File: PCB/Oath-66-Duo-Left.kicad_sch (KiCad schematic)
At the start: 67 parts, among them U1 Arduino_Pro_Micro

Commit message: PCB Updated
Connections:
- net Col 0: now also U1.16 (15/PB1); no longer U1.8 (5/PC6)
- net Col 1: now also U1.5 (2/PD1); no longer U1.10 (7/PE6)
- net Col 2: now also U1.7 (4/PD4); no longer U1.11 (8/PB4)
- net Col 3: now also U1.9 (6/PD7); no longer U1.15 (14/PB3)
- net Col 4: now also U1.11 (8/PB4); no longer U1.13 (10/PB6)
- net Col 5: now also U1.13 (10/PB6); no longer U1.5 (2/PD1)
- net Col 6: now also U1.14 (16/PB2); no longer U1.6 (3/PD0)
- net Row 0: now also U1.15 (14/PB3); no longer U1.7 (4/PD4)
- net Row 1: now also U1.6 (3/PD0); no longer U1.9 (6/PD7)
- net Row 2: now also U1.8 (5/PC6); no longer U1.12 (9/PB5)
- net Row 3: now also U1.10 (7/PE6); no longer U1.16 (15/PB1)
- net Row 4: now also U1.12 (9/PB5); no longer U1.14 (16/PB2)

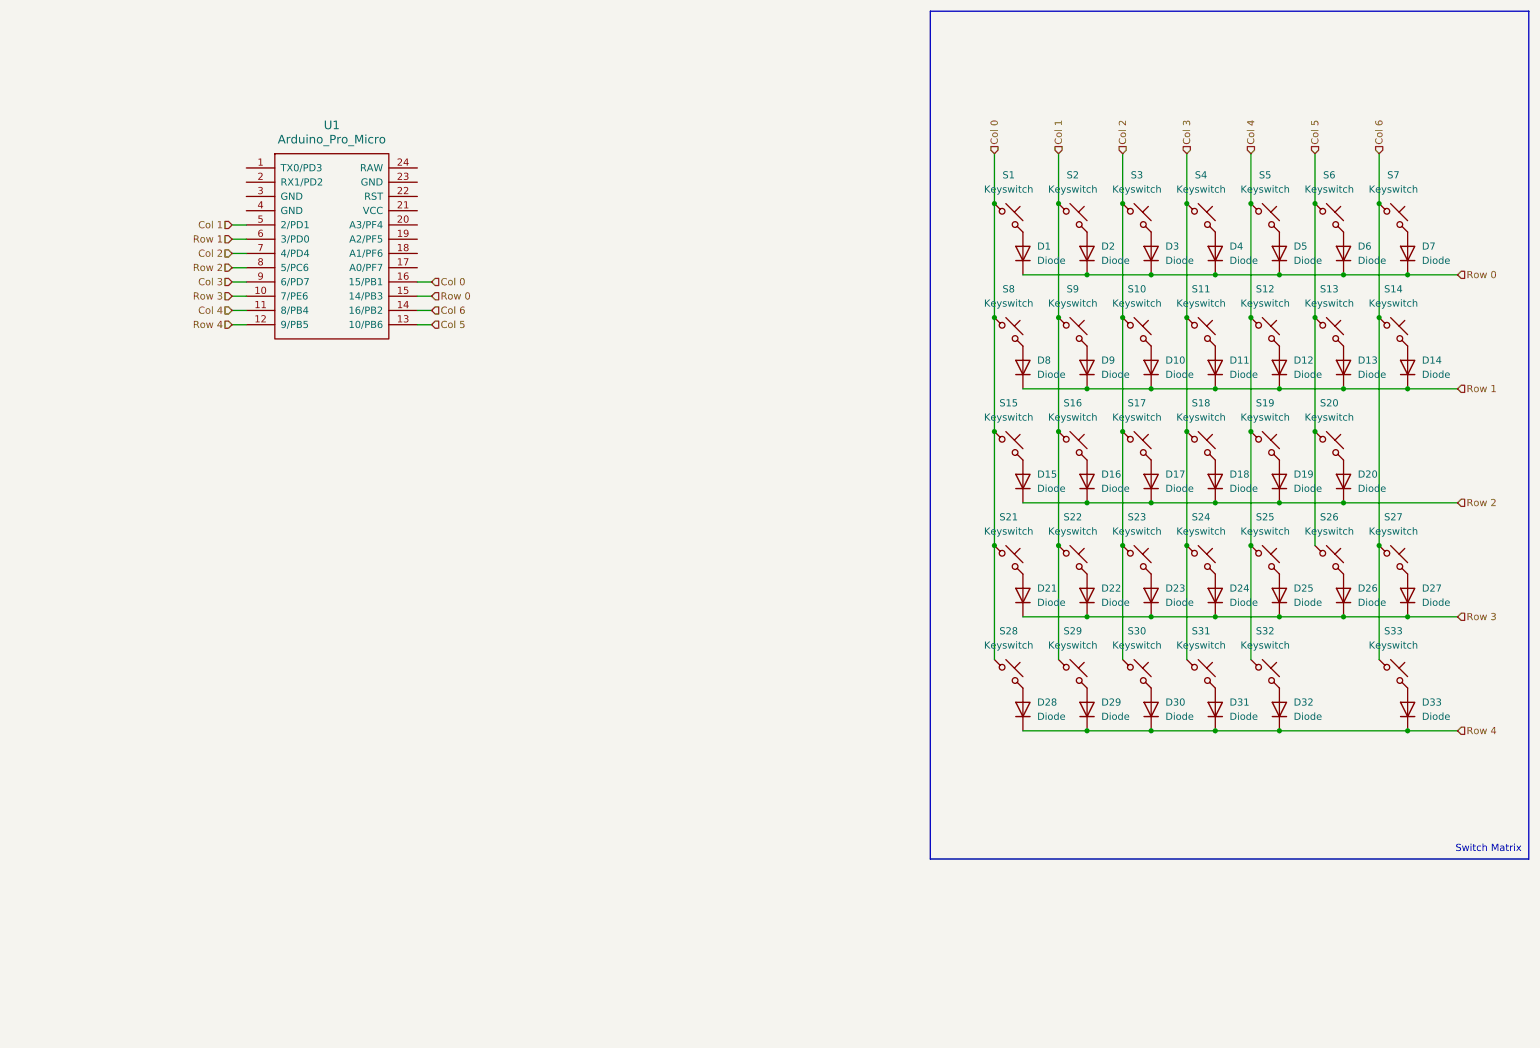
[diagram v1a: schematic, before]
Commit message: Schematic and PCB Updated
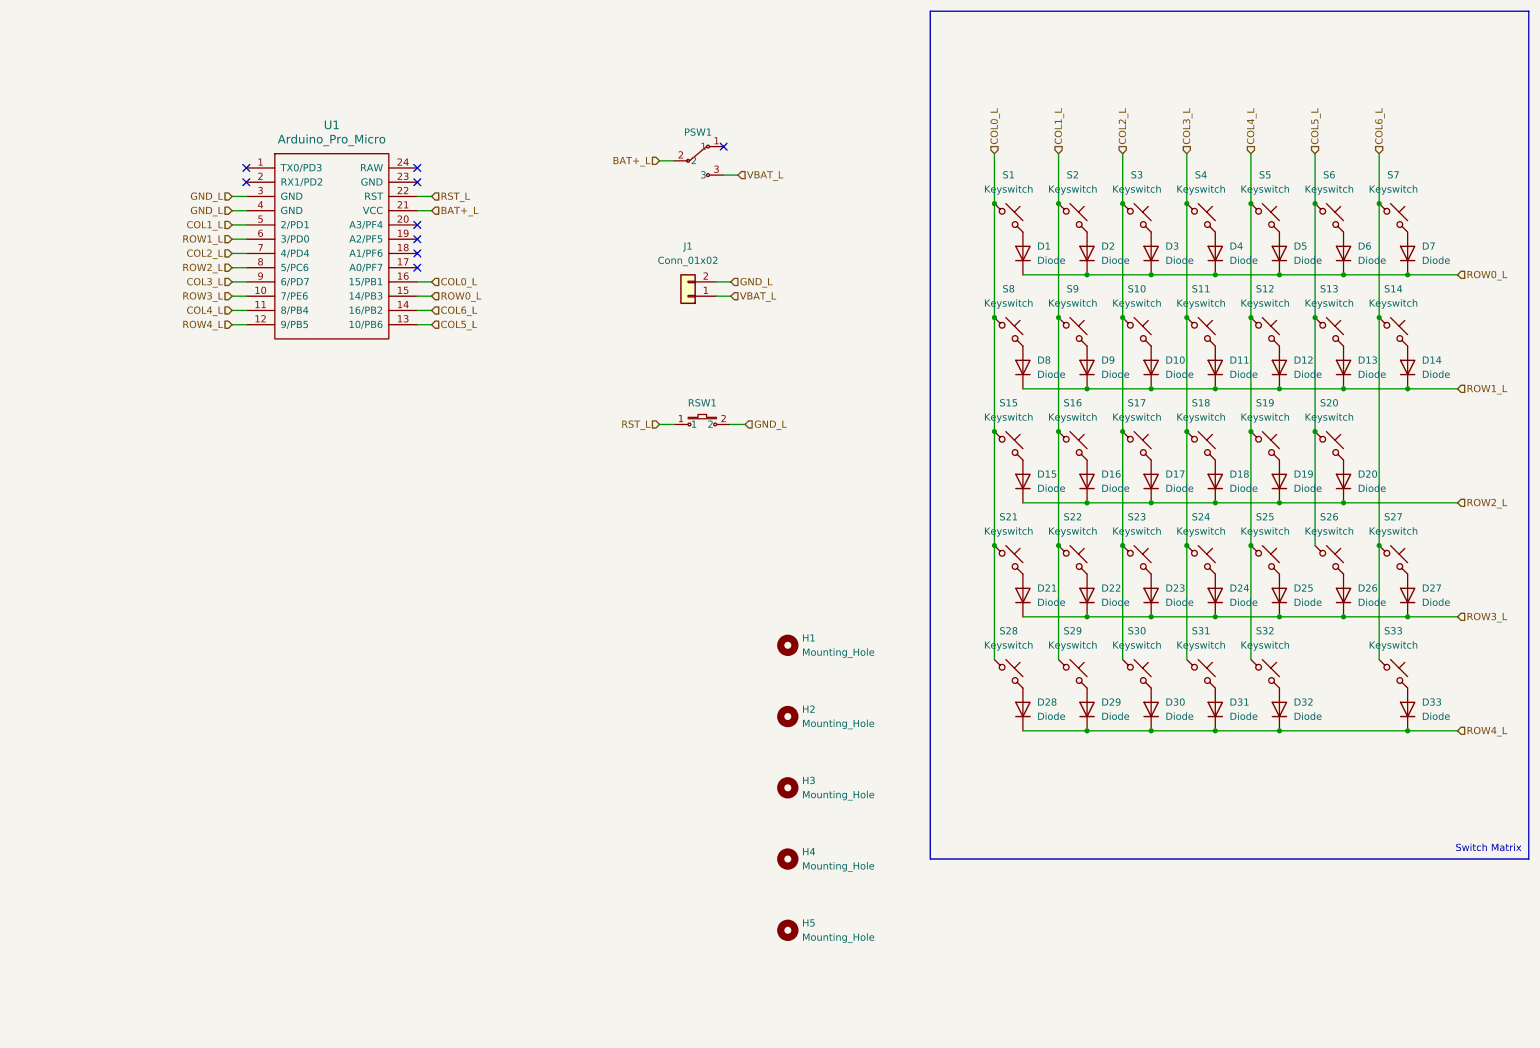
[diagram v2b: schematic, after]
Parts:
- added H1, H2, H3, H4, H5: Mounting_Hole, MountingHole:MountingHole_2.5mm, symbol ScottoKeebs:Placeholder_Mounting_Hole
- added J1: Conn_01x02, Connector_JST:JST_PH_S2B-PH-K_1x02_P2.00mm_Horizontal, symbol Connector_Generic:Conn_01x02
- added PSW1: ~, MyLibrary:MSK_1134_3PIN_2H, symbol MyLibrary:MSK_1134_3PIN_2H
- added RSW1: ~, MyLibrary:Tactile_Switch_3_6_2.5mm, symbol MyLibrary:Tactile_Swtich_3*6*2.5mm
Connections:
- net BAT+_L: now reaches U1.21 (VCC)
- net BAT+_L: now also PSW1.2
- net RST_L: now reaches U1.22 (RST)
- net RST_L: now also RSW1.1
- net GND_L: now reaches U1.3 (GND)
- net GND_L: now also U1.4 (GND), J1.2 (Pin_2), RSW1.2
- net Col 0 renamed COL0_L
- net Col 1 renamed COL1_L
- net Col 2 renamed COL2_L
- net Col 3 renamed COL3_L
- net Col 4 renamed COL4_L
- net Col 5 renamed COL5_L
- net Col 6 renamed COL6_L
- net Row 0 renamed ROW0_L
- net Row 1 renamed ROW1_L
- net Row 2 renamed ROW2_L
- net Row 3 renamed ROW3_L
- net Row 4 renamed ROW4_L
- new net VBAT_L: J1.1 (Pin_1), PSW1.3
- no-connect marks 0 -> 9

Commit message: PCB Routing Finished
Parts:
- removed J1: Conn_01x02, Connector_JST:JST_PH_S2B-PH-K_1x02_P2.00mm_Horizontal, symbol Connector_Generic:Conn_01x02
- added J1: Connector_PH2.0_2Pin_Horizontal, Connector_JST:JST_GH_SM02B-GHS-TB_1x02-1MP_P1.25mm_Horizontal, symbol MyLibrary:Connector_PH2.0_2Pin_Horizontal
- PSW1: footprint MyLibrary:MSK_1134_3PIN_2H -> MyLibrary:MSK_1134_3Pin_2H; symbol MyLibrary:MSK_1134_3PIN_2H -> MyLibrary:MSK_1134_3Pin_2H
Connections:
- net GND_L: now also U1.23 (GND), J1.2 (Pin_2)
- net VBAT_L: now also J1.1 (Pin_1)
- no-connect marks 9 -> 10
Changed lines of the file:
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@@
 	)
 	(no_connect
+		(at 134.62 57.15)
+	)
+	(no_connect
 		(at 55.88 44.45)
 	)
@@
 	)
 	(no_connect
-		(at 86.36 41.91)
+		(at 134.62 69.85)
 	)
 	(no_connect
-		(at 86.36 57.15)
+		(at 86.36 41.91)
 	)
 	(no_connect
-		(at 86.36 44.45)
+		(at 86.36 57.15)
 	)
 	(wire
@@
 	(wire
 		(pts
+			(xy 88.9 44.45) (xy 86.36 44.45)
+		)
+		(stroke
+			(width 0)
+			(type default)
+		)
+	)
+	(wire
+		(pts
 			(xy 189.23 48.26) (xy 189.23 68.58)
 		)
@@
 		)
 	)
+	(hierarchical_label "GND_L"
+		(shape input)
+		(at 88.9 44.45 0)
+		(effects
+			(font
+				(size 1.27 1.27)
+			)
+			(justify left)
+		)
+	)
 	(hierarchical_label "ROW2_L"
 		(shape input)
@@
 	)
 	(symbol
-		(lib_id "Connector_Generic:Conn_01x02")
-		(at 134.62 64.77 180)
-		(unit 1)
-		(exclude_from_sim no)
-		(in_bom yes)
-		(on_board yes)
-		(dnp no)
-		(fields_autoplaced yes)
-		(property "Reference" "J1"
-			(at 134.62 55.88 0)
-			(effects
-				(font
-					(size 1.27 1.27)
-				)
-			)
-		)
-		(property "Value" "Conn_01x02"
-			(at 134.62 58.42 0)
-			(effects
-				(font
-					(size 1.27 1.27)
-				)
-			)
-		)
-		(property "Footprint" "Connector_JST:JST_PH_S2B-PH-K_1x02_P2.00mm_Horizontal"
-			(at 134.62 64.77 0)
-			(effects
-				(font
-					(size 1.27 1.27)
-				)
-				(hide yes)
-			)
-		)
-		(property "Datasheet" "~"
-			(at 134.62 64.77 0)
-			(effects
-				(font
-					(size 1.27 1.27)
-				)
-				(hide yes)
-			)
-		)
-		(property "Description" "Generic connector, single row, 01x02, script generated (kicad-library-utils/schlib/autogen/connector/)"
-			(at 134.62 64.77 0)
-			(effects
-				(font
-					(size 1.27 1.27)
-				)
-				(hide yes)
-			)
-		)
-		(pin "1"
-		)
-		(pin "2"
-		)
-		(instances
-			(project ""
-				(path "/79e2eb2a-25a9-43ec-81b5-27be6f17dde1/dc66a3f1-360c-49e0-a707-da2ad99d4a23"
-					(reference "J1")
-					(unit 1)
-				)
-			)
-		)
-	)
-	(symbol
 		(lib_id "ScottoKeebs:Placeholder_Mounting_Hole")
 		(at 152.4 139.7 0)
@@
 	)
 	(symbol
+		(lib_id "MyLibrary:Connector_PH2.0_2Pin_Horizontal")
+		(at 135.89 63.5 180)
+		(unit 1)
+		(exclude_from_sim no)
+		(in_bom yes)
+		(on_board yes)
+		(dnp no)
+		(fields_autoplaced yes)
+		(property "Reference" "J1"
+			(at 132.08 62.2299 0)
+			(effects
+				(font
+					(size 1.27 1.27)
+				)
+				(justify left)
+			)
+		)
+		(property "Value" "Connector_PH2.0_2Pin_Horizontal"
+			(at 132.08 64.7699 0)
+			(effects
+				(font
+					(size 1.27 1.27)
+				)
+				(justify left)
+			)
+		)
+		(property "Footprint" "Connector_JST:JST_GH_SM02B-GHS-TB_1x02-1MP_P1.25mm_Horizontal"
+			(at 135.89 63.5 0)
+			(effects
+				(font
+					(size 1.27 1.27)
+				)
+				(hide yes)
+			)
+		)
+		(property "Datasheet" ""
+			(at 135.89 63.5 0)
+			(effects
+				(font
+					(size 1.27 1.27)
+				)
+				(hide yes)
+			)
+		)
+		(property "Description" "PH2.0接插件2PIN卧贴"
+			(at 136.144 50.8 0)
+			(effects
+				(font
+					(size 1.27 1.27)
+				)
+				(hide yes)
+			)
+		)
+		(pin "MP"
+		)
+		(pin "2"
+		)
+		(pin "MP"
+		)
+		(pin "1"
+		)
+		(instances
+			(project ""
+				(path "/79e2eb2a-25a9-43ec-81b5-27be6f17dde1/dc66a3f1-360c-49e0-a707-da2ad99d4a23"
+					(reference "J1")
+					(unit 1)
+				)
+			)
+		)
+	)
+	(symbol
 		(lib_id "ScottoKeebs:Placeholder_Diode")
 		(at 205.74 77.47 90)
@@
 	)
 	(symbol
-		(lib_id "MyLibrary:MSK_1134_3PIN_2H")
+		(lib_id "MyLibrary:MSK_1134_3Pin_2H")
 		(at 134.62 40.64 0)
 		(unit 1)
@@
 			)
 		)
-		(property "Footprint" "MyLibrary:MSK_1134_3PIN_2H"
+		(property "Footprint" "MyLibrary:MSK_1134_3Pin_2H"
 			(at 134.62 50.546 0)
 			(effects

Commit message: Bug Fixed
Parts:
- removed U1: Arduino_Pro_Micro, ScottoKeebs_MCU:Arduino_Pro_Micro, symbol ScottoKeebs:MCU_Arduino_Pro_Micro
- added U1: nice_nano, PCM_marbastlib-xp-promicroish:nice_nano_AH_USBup, symbol PCM_marbastlib-promicroish:nice_nano
- J1: value Connector_PH2.0_2Pin_Horizontal -> GH1.25 Battery Connector
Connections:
- net BAT+_L: now also U1.29 (BAT+)
- net COL0_L: now also U1.21 (P1.13-LF)
- net COL1_L: now also U1.5 (P0.17)
- net COL2_L: now also U1.7 (P0.22)
- net COL3_L: now also U1.9 (P1.00)
- net COL4_L: now also U1.11 (P1.04-LF)
- net COL5_L: now also U1.24 (P0.09-LF)
- net COL6_L: now also U1.23 (P0.10-LF)
- net GND_L: now also U1.14 (GND), U1.28 (GND), U1.3 (GND), U1.4 (GND)
- net ROW0_L: now also U1.22 (P1.11-LF)
- net ROW1_L: now also U1.6 (P0.20)
- net ROW2_L: now also U1.8 (P0.24)
- net ROW3_L: now also U1.10 (P0.11)
- net ROW4_L: now also U1.12 (P1.06-LF)
- net RST_L: now also U1.15 (RST)
- no-connect marks 10 -> 13
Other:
- note added: "Battery Connector and Power Switch"
- note added: "Mounting Hole"
- note added: "Nice Nano V2"
- note added: "Oath 66 Duo"
- note added: "Reset Button"
- note added: "with dongle"
- moved on the sheet: H1, H2, H3, H4, H5, PSW1, RSW1

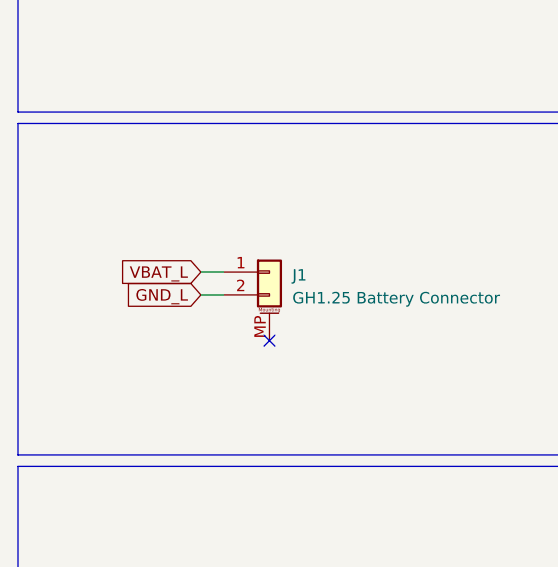
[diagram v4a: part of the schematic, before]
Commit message: Battery Connector Updated
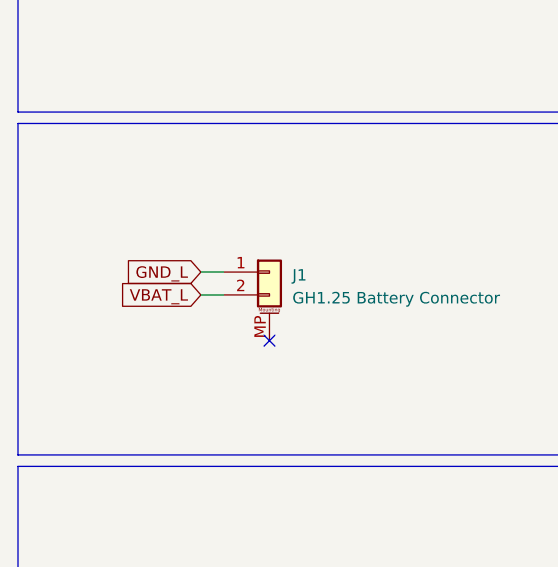
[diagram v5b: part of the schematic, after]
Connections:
- net GND_L: now also J1.1 (Pin_1); no longer J1.2 (Pin_2)
- net VBAT_L: now also J1.2 (Pin_2); no longer J1.1 (Pin_1)
